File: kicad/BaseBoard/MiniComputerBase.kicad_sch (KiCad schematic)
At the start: 32 parts, among them J1 VIN, J2 PWRALT, J3 RESET, SW1 POWER, SW2 RESET, U1 L78L33, U2 LM7805, U3 DS1813-5+, U4 W65C02SxP, X1 XTAL, X2 XTAL_ALT

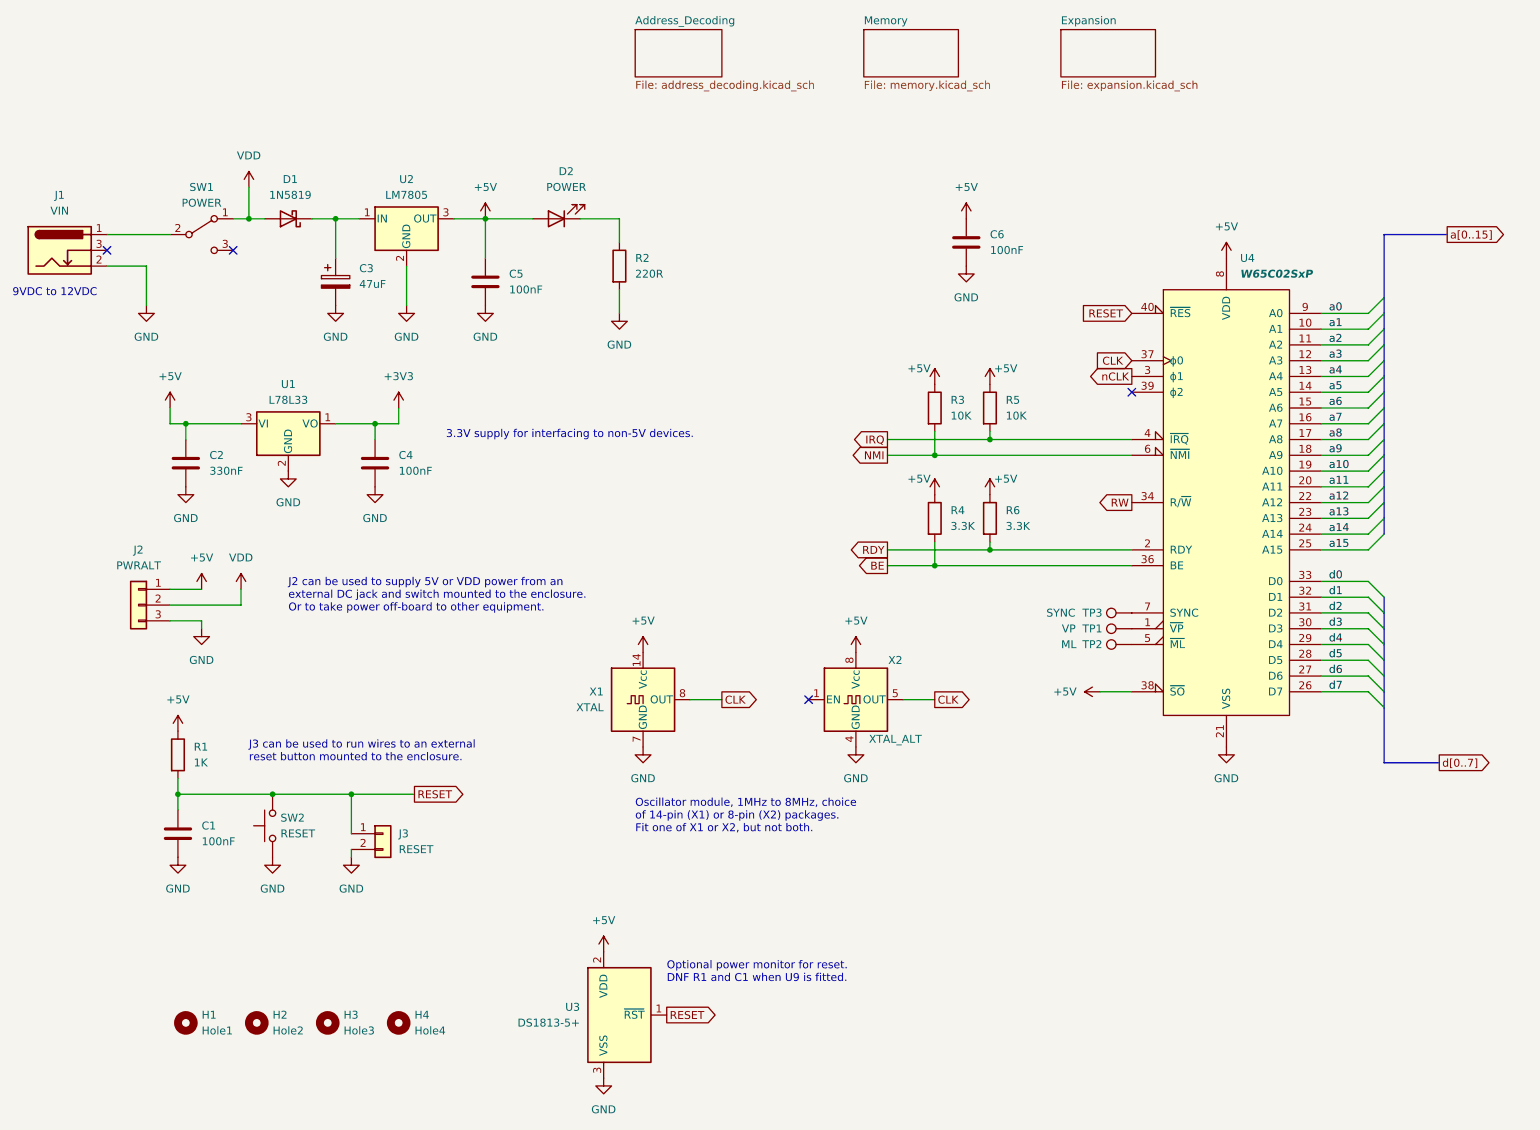
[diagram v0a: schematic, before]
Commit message: I/O board schematic and layout
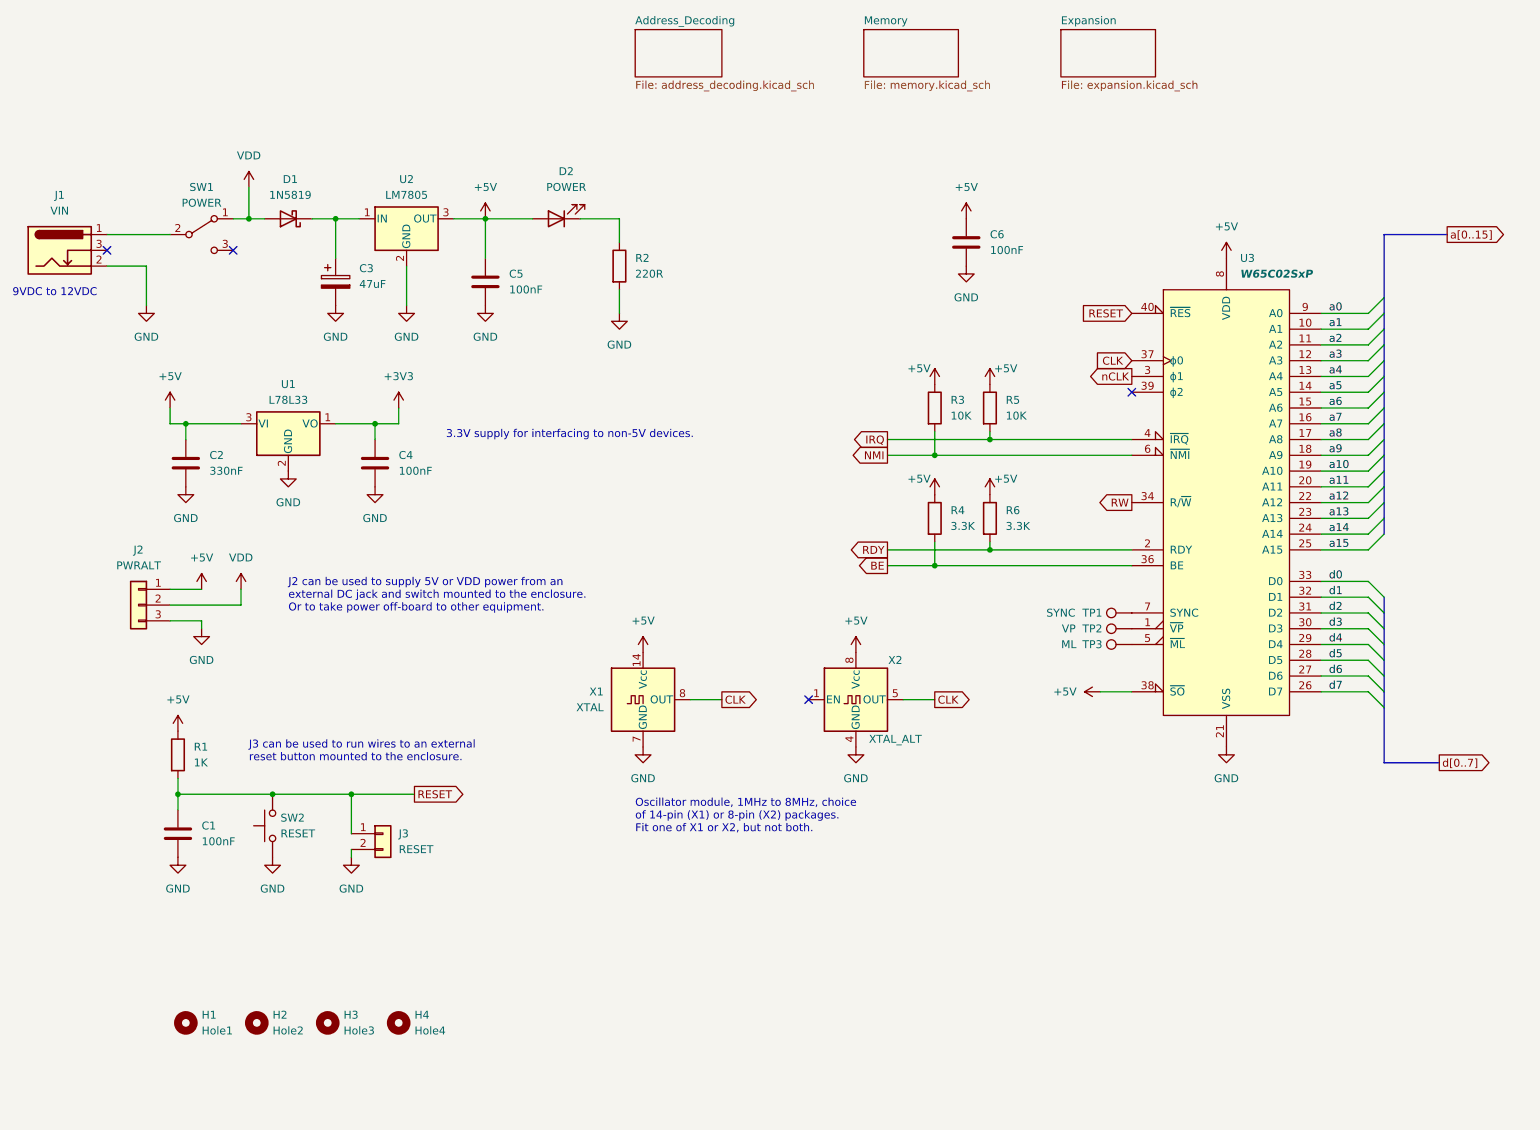
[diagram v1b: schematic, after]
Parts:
- removed U3: DS1813-5+, Package_TO_SOT_THT:TO-92_Inline, symbol Power_Supervisor:MCP100-270D
- renumbered TP3 to TP1, TP1 to TP2, TP2 to TP3, U4 to U3
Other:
- note removed: "Optional power monitor for reset. DNF R1 and C1 when U9 is fitted."

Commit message: Documentation
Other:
- note added: "Use 220R or 1K depending upon LED type."
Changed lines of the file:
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@@
+    (effects (font (size 1.27 1.27)) (justify left bottom))
+  )
+  (text "Use 220R or 1K depending upon LED type." (at 125.73 62.23 0)
     (effects (font (size 1.27 1.27)) (justify left bottom))
   )

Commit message: Component updates after first build
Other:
- note removed: "Use 220R or 1K depending upon LED type."
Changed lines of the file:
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@@
-    (effects (font (size 1.27 1.27)) (justify left bottom))
-  )
-  (text "Use 220R or 1K depending upon LED type." (at 125.73 62.23 0)
     (effects (font (size 1.27 1.27)) (justify left bottom))
   )
